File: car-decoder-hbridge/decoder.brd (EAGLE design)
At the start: 98.8 x 80 mm, 51 parts, among them U2 RFM69CW, U3 MCP73831, U4 ATMEGA328P, U6 MIC5219 3.3V, Y1 16MHZ

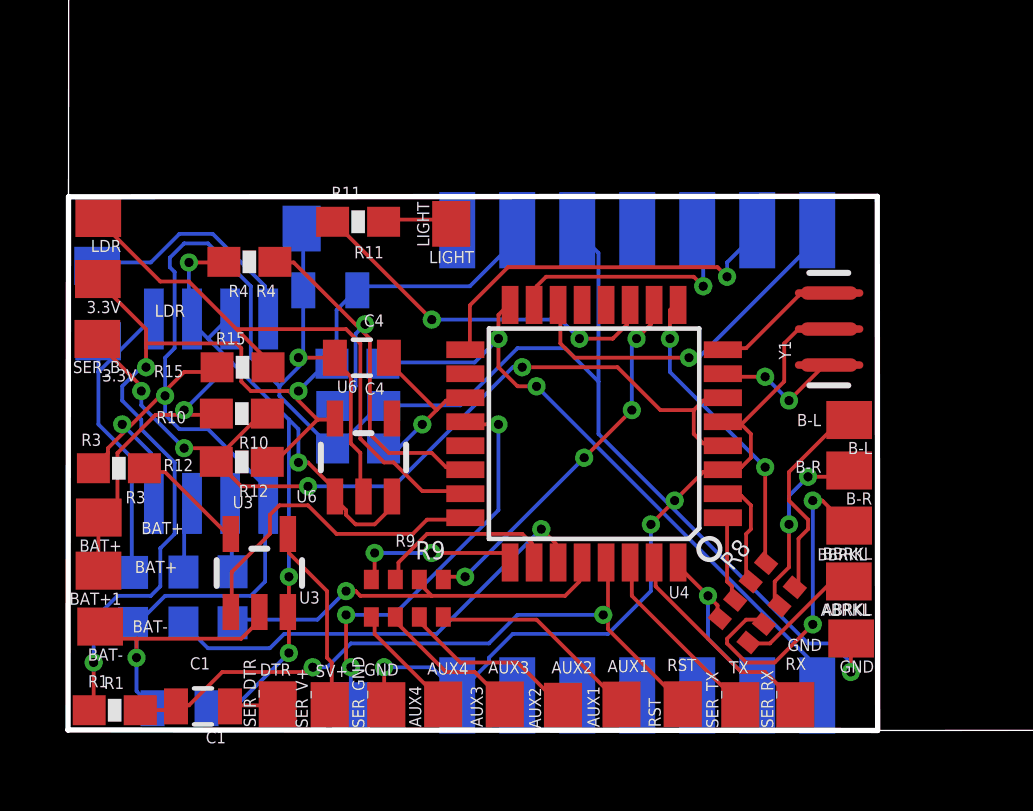
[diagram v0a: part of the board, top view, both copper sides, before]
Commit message: some board simplification and isolation of motor speed sensor
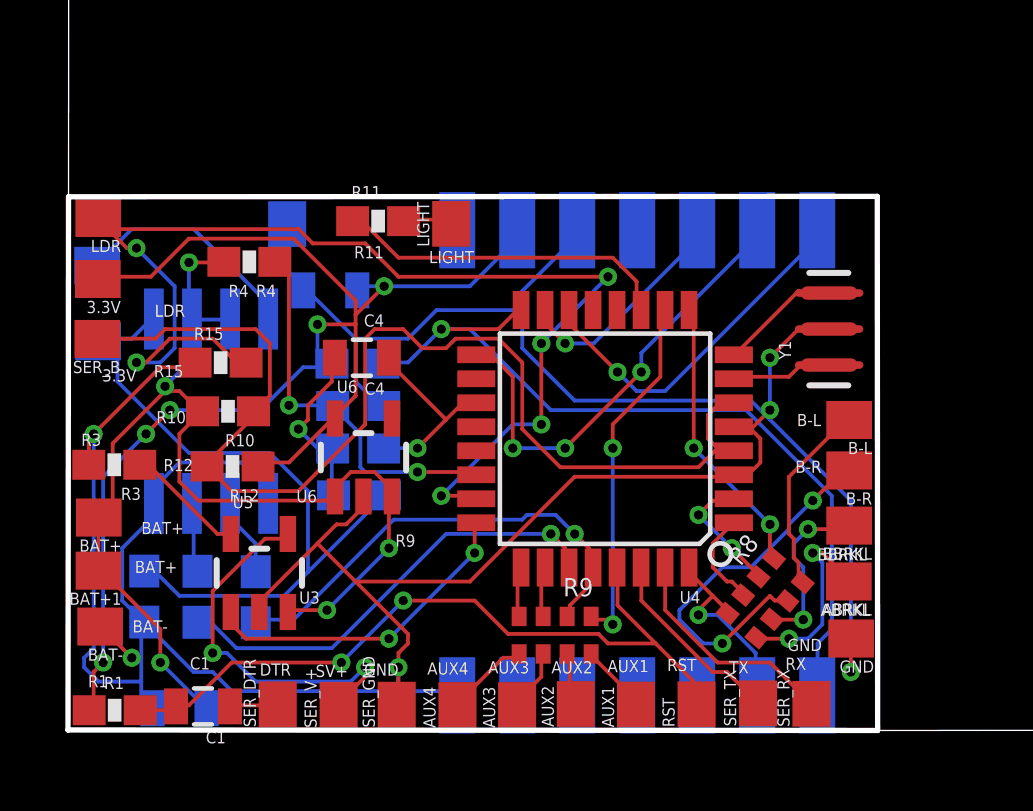
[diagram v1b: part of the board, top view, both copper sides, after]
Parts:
- removed 2.56V: (no value), wirepad:SMD1,27-2,54
- added R16: 0, SparkFun-Resistors:0603-RES
- moved R9 5.08 mm to (17.4, 3.13)
- moved R6 0.77 mm to (7.47, 4.40)
- moved R15 0.75 mm to (6.30, 12.2)
- moved R11 0.67 mm to (11.5, 16.9)
- moved SER_TX 0.60 mm to (24.2, 0.86)
- moved SER_RX 0.54 mm to (26.0, 0.84)
- moved GND1 0.50 mm to (8.52, 16.8)
- moved AUX1 0.48 mm to (20.1, 0.83)
- moved AUX4 0.48 mm to (14.2, 0.81)
- moved R7 0.47 mm to (5.53, 4.41)
- moved R10 0.47 mm to (6.54, 10.6)
- moved RST 0.46 mm to (22.2, 0.83)
- moved AUX2 0.43 mm to (18.1, 0.84)
- moved AUX3 0.41 mm to (16.2, 0.81)
- moved U4 0.40 mm to (19.1, 9.68)
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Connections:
- new net N$1: C4.2, R16.1, R2.2
- net AREF: no longer 2.56V.1
- net GND: no longer C4.2, R2.2
- net OA: now also R16.2
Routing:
- net A0: track 19.7 -> 40.6 mm, vias 0 -> 6
- net OA: track 10.8 -> 24.6 mm
- net AREF: track 13.6 -> 0.00 mm, vias 3 -> 0
- net N$8: track 31.0 -> 39.5 mm, vias 4 -> 0
- net N$1: track 0.00 -> 6.49 mm, vias 0 -> 1
- net N$16: track 6.35 -> 12.7 mm
- net N$9: track 6.31 -> 12.7 mm, vias 0 -> 2
- net VCC: track 39.4 -> 45.7 mm, vias 3 -> 5
- net MISO: track 22.2 -> 27.5 mm, vias 2 -> 1
- net N$18: track 11.0 -> 5.82 mm
- net N$21: track 7.14 -> 2.30 mm
- net A3: track 6.24 -> 1.70 mm
- net N$22: track 6.10 -> 1.77 mm
- net A2: track 5.62 -> 1.69 mm, vias 2 -> 0
- net N$23: track 4.97 -> 2.04 mm
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
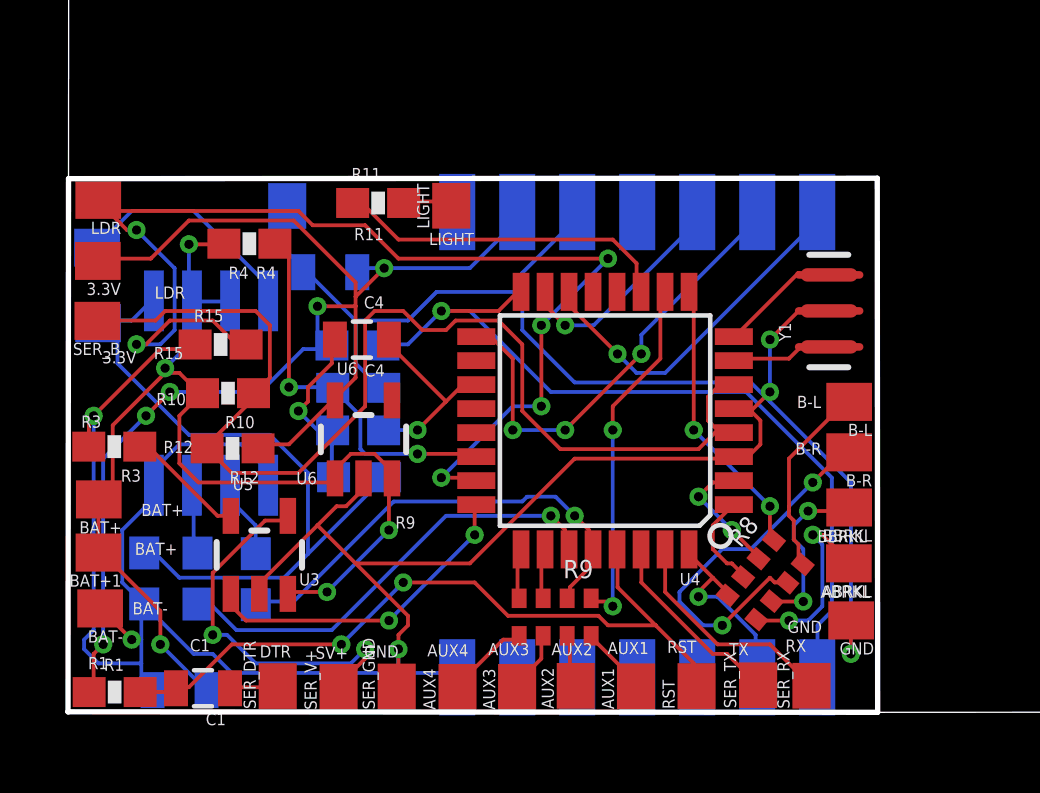
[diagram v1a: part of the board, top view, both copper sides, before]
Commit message: New layout for RFM69HC
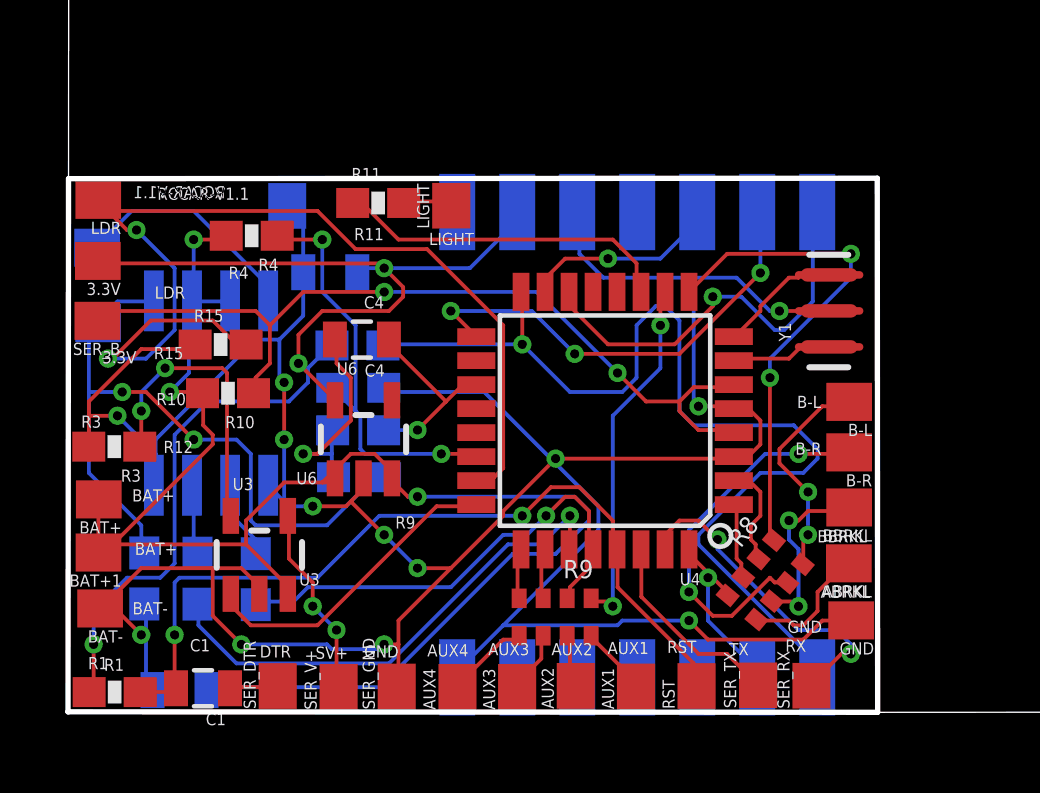
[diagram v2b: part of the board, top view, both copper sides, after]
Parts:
- removed R12: 0, SparkFun-Resistors:0603-RES
- moved R4 0.28 mm to (7.33, 15.8)
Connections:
- net N$8: no longer R12.2
- net VCC: no longer R12.1
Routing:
- net BAT+: track 38.9 -> 55.2 mm, vias 5 -> 3
- net N$8: track 39.5 -> 28.7 mm, vias 0 -> 2
- net MISO: track 27.5 -> 34.6 mm
- net BL: track 9.60 -> 16.7 mm
- net N$9: track 12.7 -> 6.38 mm
- net N$11: track 4.00 -> 9.98 mm, vias 0 -> 2
- net A0: track 40.6 -> 34.7 mm, vias 6 -> 2
- net VCC: track 45.7 -> 41.7 mm, vias 5 -> 3
- net TX: track 7.59 -> 10.9 mm, vias 0 -> 2
- net N$5: track 25.0 -> 27.9 mm
- net N$20: track 6.53 -> 4.38 mm, vias 2 -> 0
- net SS: track 12.1 -> 13.9 mm
- net GND: track 115.1 -> 116.8 mm, vias 6 -> 13
- net A4: track 15.2 -> 16.8 mm
- net A7: track 12.9 -> 14.2 mm
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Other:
- board text added: "RCCAR-V1.1"
